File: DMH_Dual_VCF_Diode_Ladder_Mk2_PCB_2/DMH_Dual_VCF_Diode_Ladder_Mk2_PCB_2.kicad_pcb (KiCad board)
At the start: 2 copper layers, 146 x 175 mm, 70 parts, among them J15 Conn_01x08_PinHeader, J16 Conn_01x08_PinHeader, J17 Conn_01x06_PinHeader, J18 Conn_01x06_PinHeader, J19 Conn_01x06_PinHeader, J20 Conn_01x06_PinHeader, J21 Conn_01x06_PinHeader, J22 Conn_01x06_PinHeader, J23 Conn_01x04_PinHeader, SW1 SW_SPDT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

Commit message: Mistakes found during assembly
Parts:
- R111, R128: value 20k -> 10k
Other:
- board text added: "Was 20k in Mk2 v1 Gerber by mistake"
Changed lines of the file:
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@@
 		)
 		(property "Datasheet" ""
-			(at 0 0 -90)
+			(at 0 0 270)
 			(unlocked yes)
 			(layer "F.Fab")
@@
 		)
 		(property "Description" "Resistor, US symbol"
-			(at 0 0 -90)
+			(at 0 0 270)
 			(unlocked yes)
 			(layer "F.Fab")
@@
 			)
 		)
-		(property "Value" "20k"
+		(property "Value" "10k"
 			(at 3.81 0 180)
 			(layer "F.SilkS")
@@
 			)
 		)
-		(property "Value" "20k"
+		(property "Value" "10k"
 			(at 3.81 0 180)
 			(layer "F.SilkS")
@@
 		)
 		(property "Datasheet" ""
-			(at 0 0 -90)
+			(at 0 0 270)
 			(unlocked yes)
 			(layer "F.Fab")
@@
 		)
 		(property "Description" "Resistor, US symbol"
-			(at 0 0 -90)
+			(at 0 0 270)
 			(unlocked yes)
 			(layer "F.Fab")
@@
 	)
 	(gr_circle
+		(center 154.9 90.8)
+		(end 154.8 93.8)
+		(stroke
+			(width 0.5)
+			(type default)
+		)
+		(fill no)
+		(layer "Cmts.User")
+	)
+	(gr_circle
 		(center 133.5 190.25)
 		(end 138 190.25)
@@
 		(layer "Cmts.User")
 	)
+	(gr_circle
+		(center 45.2 91.001666)
+		(end 45.1 94.001666)
+		(stroke
+			(width 0.5)
+			(type default)
+		)
+		(fill no)
+		(layer "Cmts.User")
+	)
 	(gr_line
 		(start 171.25 56.5)
@@
 		)
 	)
+	(gr_text "Was 20k in Mk2 v1 Gerber by mistake"
+		(at 142 86.4 0)
+		(layer "Cmts.User")
+		(effects
+			(font
+				(size 1 1)
+				(thickness 0.15)
+			)
+			(justify left bottom)
+		)
+	)
+	(gr_text "Was 20k in Mk2 v1 Gerber by mistake"
+		(at 32.3 86.601666 0)
+		(layer "Cmts.User")
+		(effects
+			(font
+				(size 1 1)
+				(thickness 0.15)
+			)
+			(justify left bottom)
+		)
+	)

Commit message: Changed Resonance pots to Taper C type
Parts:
- RV18, RV22: value 100k -> C100k
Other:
- board text added: "Inverted Log"
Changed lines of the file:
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@@
 			)
 		)
-		(property "Value" "100k"
+		(property "Value" "C100k"
 			(at 2.7 8.3 90)
 			(layer "F.SilkS")
@@
 			)
 		)
-		(property "Value" "100k"
+		(property "Value" "C100k"
 			(at 2.7 8.3 90)
 			(layer "F.SilkS")
@@
 		(layer "User.9")
 	)
+	(gr_text "Inverted Log"
+		(at 112.8 119.8 90)
+		(layer "F.SilkS")
+		(effects
+			(font
+				(size 1 1)
+				(thickness 0.2)
+				(bold yes)
+				(italic yes)
+			)
+			(justify left bottom)
+		)
+	)
+	(gr_text "Inverted Log"
+		(at 88.2 119.8 90)
+		(layer "F.SilkS")
+		(effects
+			(font
+				(size 1 1)
+				(thickness 0.2)
+				(bold yes)
+				(italic yes)
+			)
+			(justify left bottom)
+		)
+	)
 	(gr_text "Mk2.0 - March 2025"

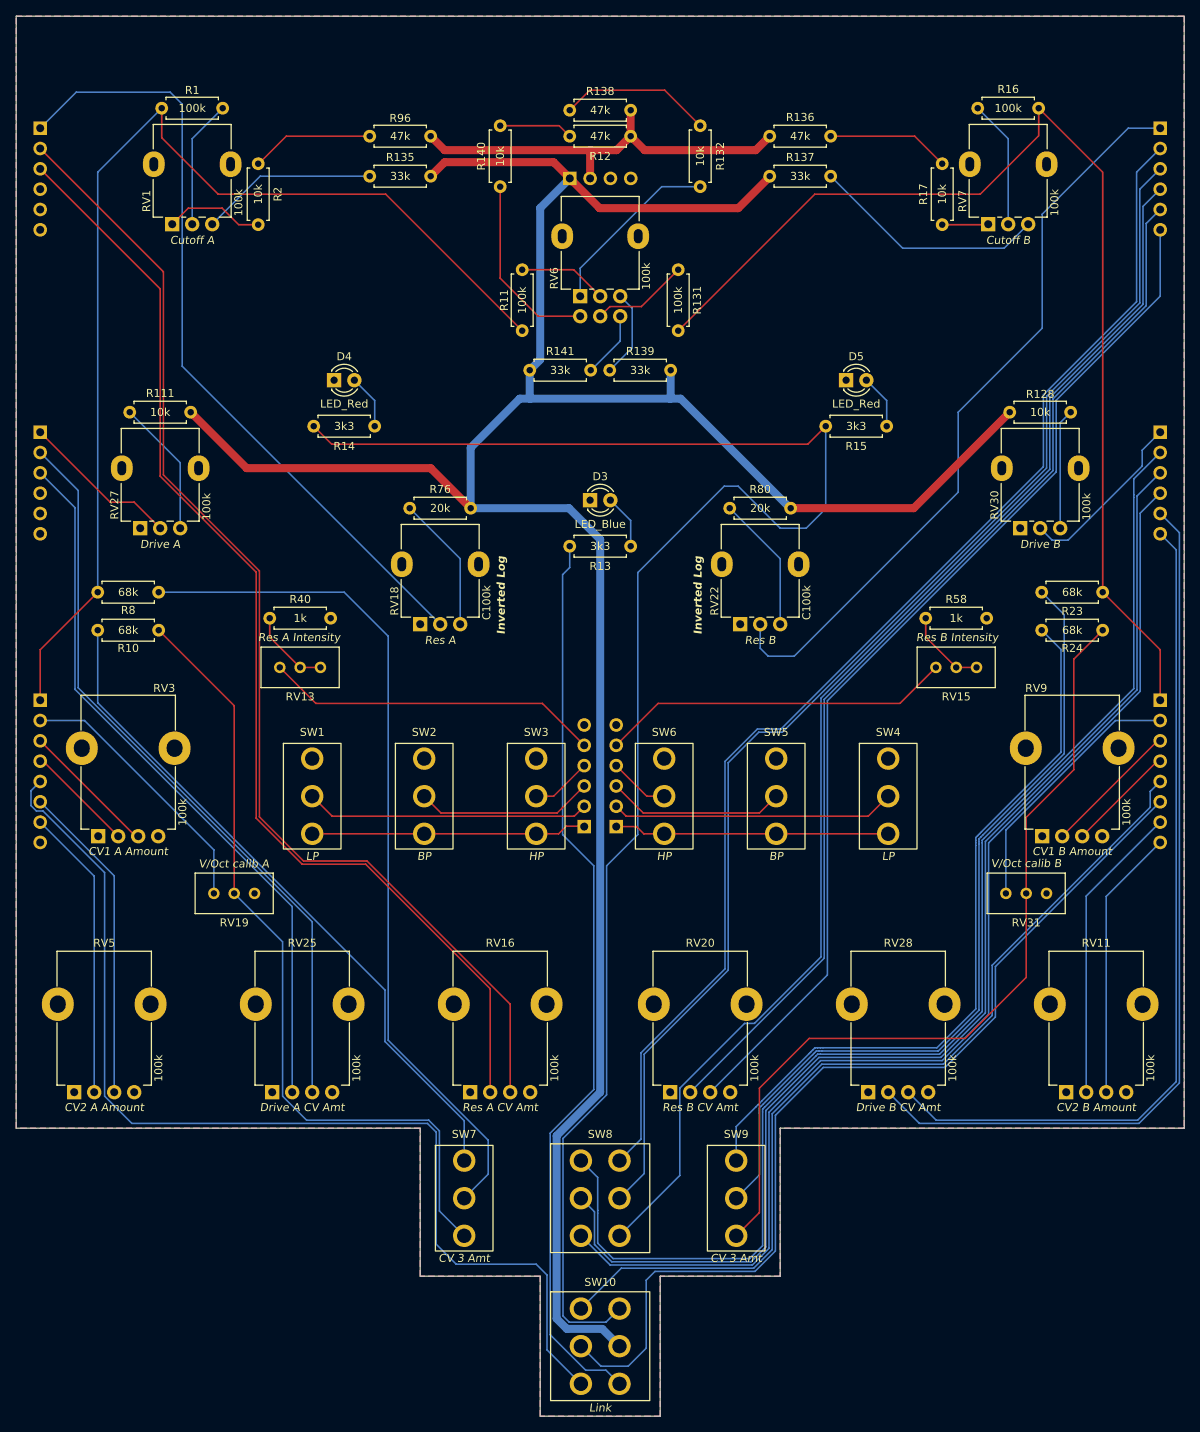
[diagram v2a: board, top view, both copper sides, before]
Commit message: KiCad 9.0.7 + centralized library
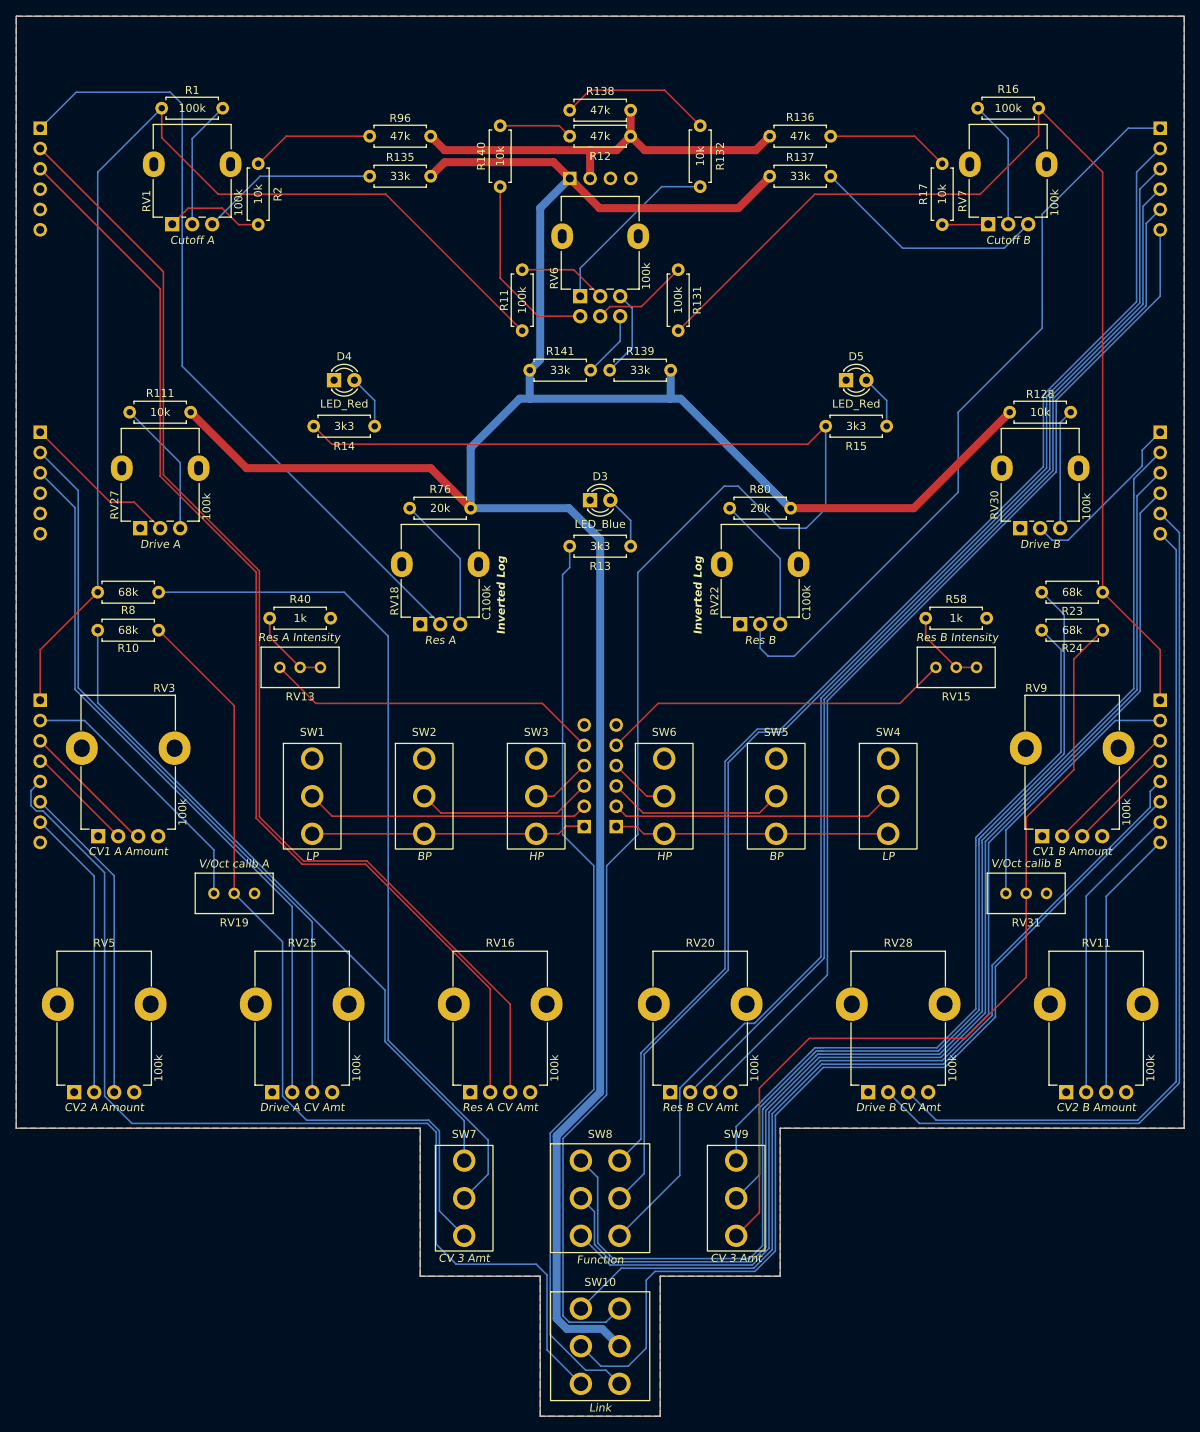
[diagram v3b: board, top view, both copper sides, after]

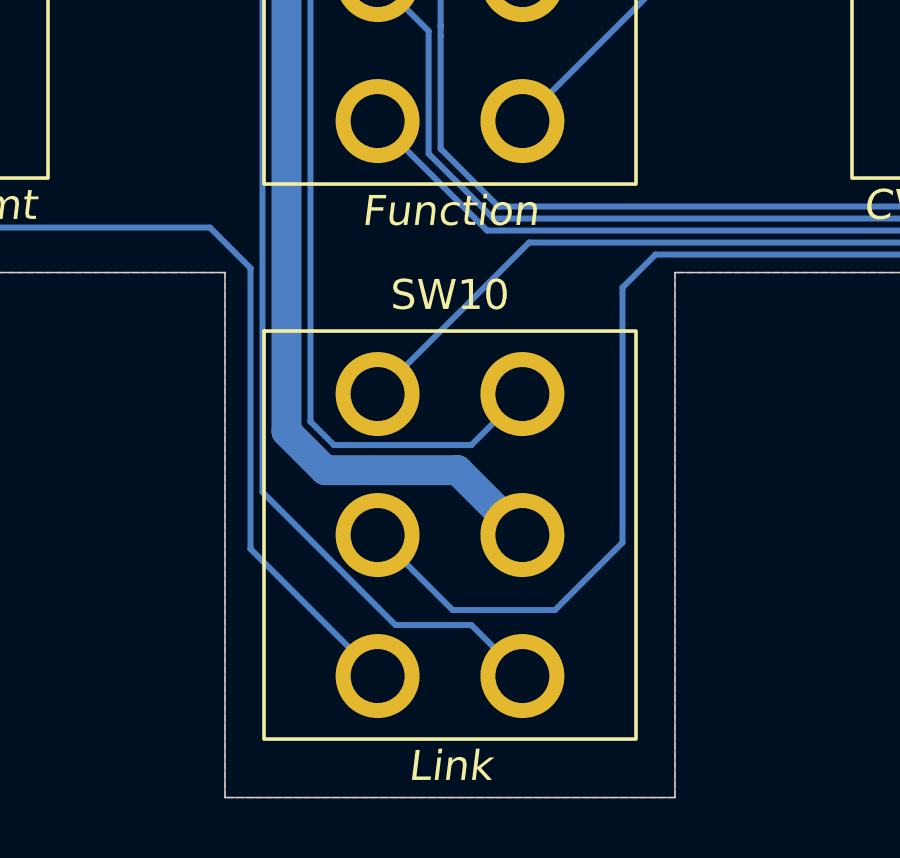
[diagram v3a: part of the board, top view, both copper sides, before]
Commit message: Re-exported Gerbers
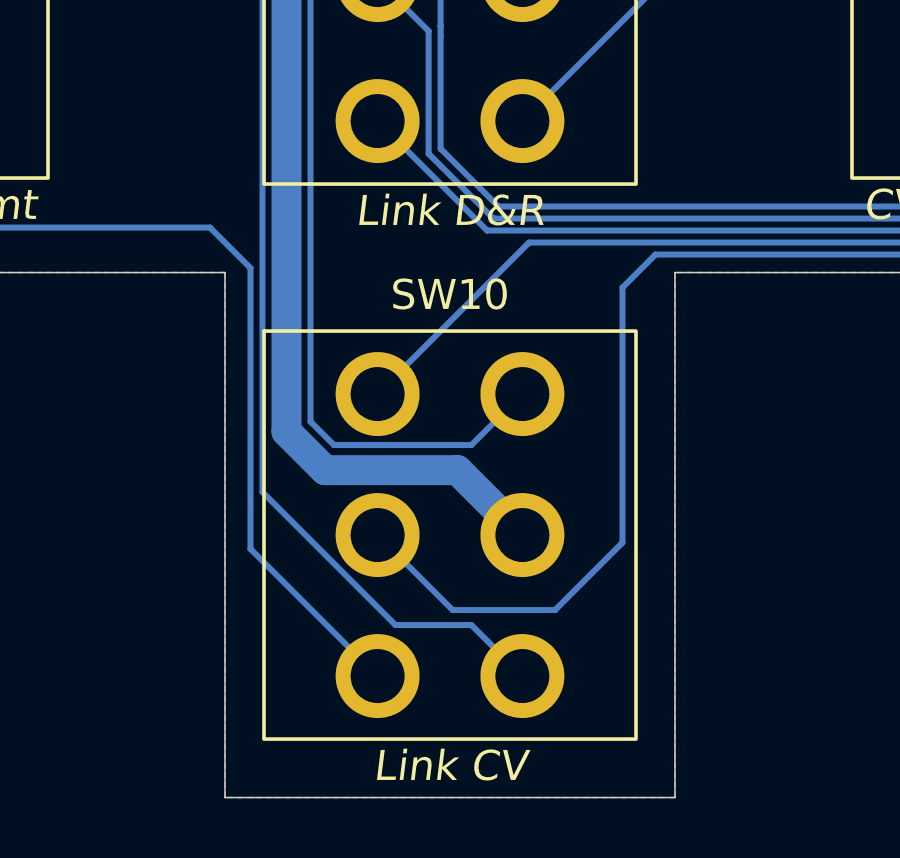
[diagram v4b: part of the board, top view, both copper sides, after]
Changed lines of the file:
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@@
 			)
 		)
-		(property "Function" "Function"
+		(property "Function" "Link D&R"
 			(at 0 7.7 0)
 			(unlocked yes)
@@
 			)
 		)
-		(property "Function" "Link"
+		(property "Function" "Link CV"
 			(at 0 7.7 0)
 			(unlocked yes)
